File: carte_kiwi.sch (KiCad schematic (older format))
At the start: 40 parts, among them IC1 MCP2562, P1 CONN_01X05, P2 CONN_01X03, P3 CONN_01X05, P4 CONN_01X03, P5 Serial Wire, P6 CAN_conn, P7 CONN_01X03, P8 CONN_01X03, P9 CAN_conn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

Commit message: Mise à jour des libs (zener, led, switch)
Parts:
- removed D1, D2, D3: ZENERsmall, Diodes_SMD:SOD-123, symbol ZENERsmall
- removed SW1: SW_PUSH_SMALL_H, Buttons_Switches_SMD:SW_SPST_EVQPE1, symbol SW_PUSH_SMALL_H
- added D1, D2, D3: D_Zener_Small, Diodes_SMD:D_SOD-123, symbol D_Zener_Small
- added SW1: SW_Push, Buttons_Switches_SMD:SW_SPST_EVQPE1, symbol SW_Push
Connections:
- wire segments 65 -> 63
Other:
- moved on the sheet: C5, D4, D5, D6, P6, P9

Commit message: corrige erreurs ERC
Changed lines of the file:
@@
 LIBS:STMicroelectronics
 LIBS:switches
-LIBS:carte_kiwi-cache
 EELAYER 25 0
 EELAYER END
@@
 	0    1    1    0
 $EndComp
+$Comp
+L PWR_FLAG #FLG055
+U 1 1 589FF92C
+P 7400 5750
+F 0 "#FLG055" H 7400 5845 50  0001 C CNN
+F 1 "PWR_FLAG" H 7400 5950 50  0000 C CNN
+F 2 "" H 7400 5750 50  0000 C CNN
+F 3 "" H 7400 5750 50  0000 C CNN
+	1    7400 5750
+	1    0    0    -1
+$EndComp
+$Comp
+L GND #PWR056
+U 1 1 589FF9B6
+P 7400 5750
+F 0 "#PWR056" H 7400 5500 50  0001 C CNN
+F 1 "GND" H 7400 5600 50  0000 C CNN
+F 2 "" H 7400 5750 50  0000 C CNN
+F 3 "" H 7400 5750 50  0000 C CNN
+	1    7400 5750
+	1    0    0    -1
+$EndComp
+$Comp
+L +9V #PWR057
+U 1 1 589FFA61
+P 7800 5700
+F 0 "#PWR057" H 7800 5550 50  0001 C CNN
+F 1 "+9V" H 7800 5840 50  0000 C CNN
+F 2 "" H 7800 5700 50  0000 C CNN
+F 3 "" H 7800 5700 50  0000 C CNN
+	1    7800 5700
+	1    0    0    -1
+$EndComp
+$Comp
+L PWR_FLAG #FLG058
+U 1 1 589FFAE4
+P 7800 5700
+F 0 "#FLG058" H 7800 5795 50  0001 C CNN
+F 1 "PWR_FLAG" H 7800 5900 50  0000 C CNN
+F 2 "" H 7800 5700 50  0000 C CNN
+F 3 "" H 7800 5700 50  0000 C CNN
+	1    7800 5700
+	-1   0    0    1
+$EndComp
 $EndSCHEMATC

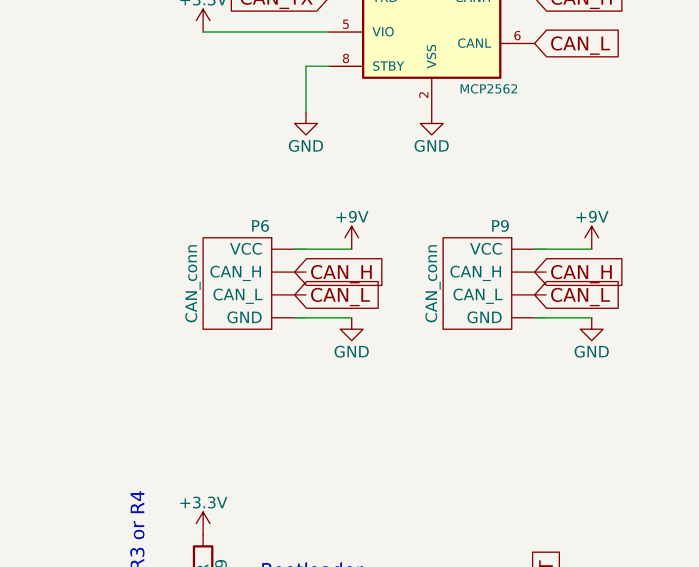
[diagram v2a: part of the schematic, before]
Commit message: retourné connecteur CAN
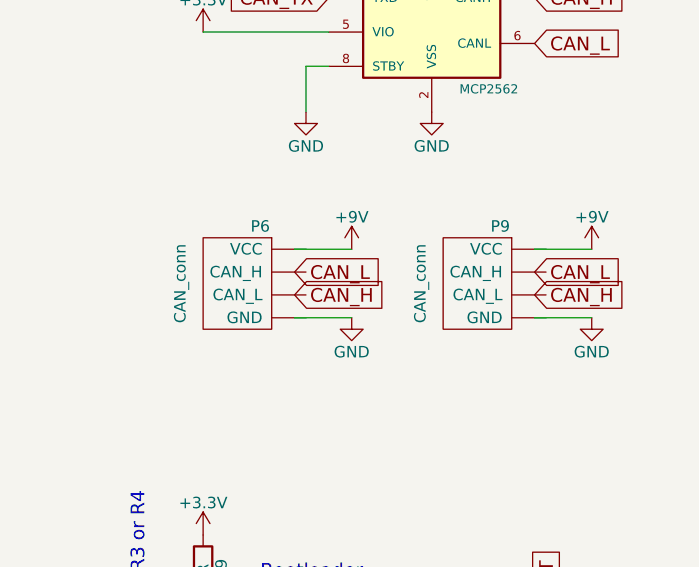
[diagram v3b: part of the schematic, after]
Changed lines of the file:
@@
 	-1   0    0    -1
 $EndComp
+Text GLabel 9400 3800 2    60   Input ~ 0
+CAN_H
 Text GLabel 9400 3700 2    60   Input ~ 0
-CAN_H
-Text GLabel 9400 3800 2    60   Input ~ 0
 CAN_L
 $Comp
@@
 Text GLabel 10500 5250 1    60   Input ~ 0
 NRST
+Text GLabel 10450 3800 2    60   Input ~ 0
+CAN_H
 Text GLabel 10450 3700 2    60   Input ~ 0
-CAN_H
-Text GLabel 10450 3800 2    60   Input ~ 0
 CAN_L
 $Comp
@@
 P 9250 3750
 F 0 "P6" H 9250 4000 50  0000 C CNN
-F 1 "CAN_conn" V 9550 3750 50  0000 C CNN
+F 1 "CAN_conn" V 9600 3750 50  0000 C CNN
 F 2 "Connectors_JST:JST_XH_B04B-XH-A_04x2.50mm_Straight" H 9250 3750 50  0001 C CNN
 F 3 "" H 9250 3750 50  0000 C CNN
@@
 P 10300 3750
 F 0 "P9" H 10300 4000 50  0000 C CNN
-F 1 "CAN_conn" V 10600 3750 50  0000 C CNN
+F 1 "CAN_conn" V 10650 3750 50  0000 C CNN
 F 2 "Connectors_JST:JST_XH_B04B-XH-A_04x2.50mm_Straight" H 10300 3750 50  0001 C CNN
 F 3 "" H 10300 3750 50  0000 C CNN

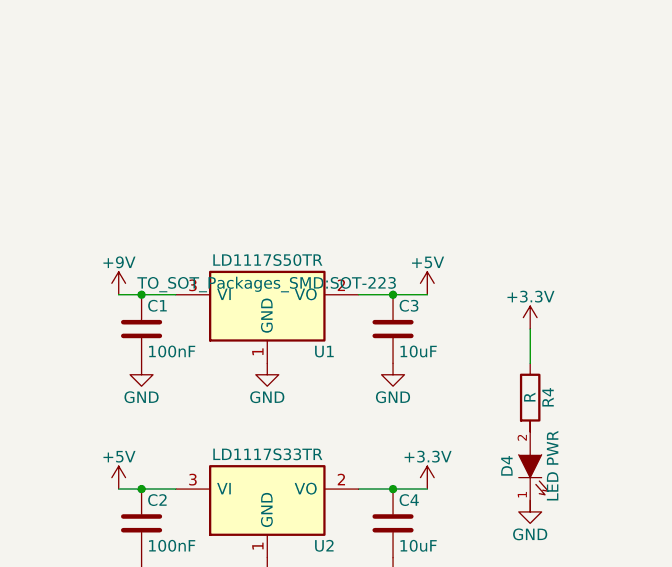
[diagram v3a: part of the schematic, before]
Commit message: updated footprint
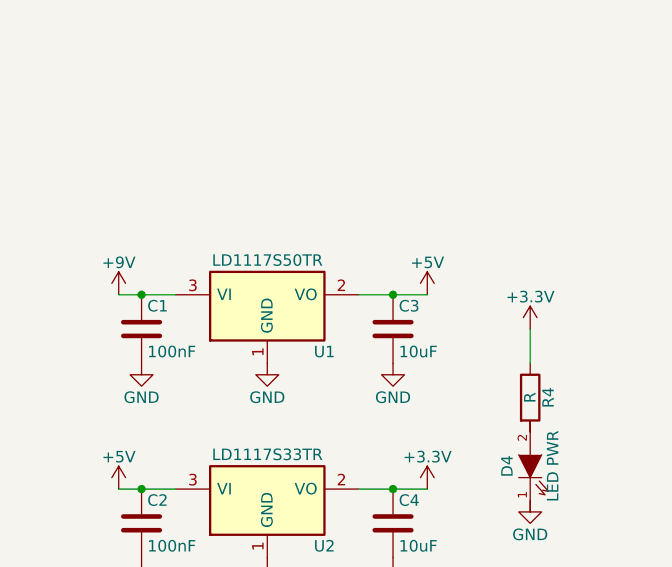
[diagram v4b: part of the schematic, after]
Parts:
- U1, U2: footprint TO_SOT_Packages_SMD:SOT-223 -> TO_SOT_Packages_SMD:SOT-223-3Lead_TabPin2
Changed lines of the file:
@@
 F 0 "U2" H 2050 6700 50  0000 C CNN
 F 1 "LD1117S33TR" H 1800 7100 50  0000 C CNN
-F 2 "TO_SOT_Packages_SMD:SOT-223" H 1800 7000 50  0001 C CNN
+F 2 "TO_SOT_Packages_SMD:SOT-223-3Lead_TabPin2" H 1800 7000 50  0001 C CNN
 F 3 "" H 1800 6900 50  0000 C CNN
 	1    1800 6900
@@
 F 0 "U1" H 2050 5850 50  0000 C CNN
 F 1 "LD1117S50TR" H 1800 6250 50  0000 C CNN
-F 2 "TO_SOT_Packages_SMD:SOT-223" H 1800 6150 50  0000 C CNN
+F 2 "TO_SOT_Packages_SMD:SOT-223-3Lead_TabPin2" H 1800 6150 50  0001 C CNN
 F 3 "" H 1800 6050 50  0000 C CNN
 	1    1800 6050

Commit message: First changes to schema. TODO : use phoenixrobotik specific libs for can_conn
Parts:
- C1, C10, C2, C3, C4, C5, C6, C7, C8, C9: symbol C -> Device:C
- D1, D2, D3: symbol D_Zener_Small -> Device:D_Zener_Small
- D4, D5, D6: symbol LED -> Device:LED
- IC1: symbol MCP2562 -> Interface_CAN_LIN:MCP2562-E-P
- P1, P3: value CONN_01X05 -> Connector_Generic:Conn_01x05; symbol CONN_01X05 -> Connector_Generic:Conn_01x05
- P2, P4, P7, P8: value CONN_01X03 -> Connector_Generic:Conn_01x03; symbol CONN_01X03 -> Connector_Generic:Conn_01x03
- P5: symbol CONN_01X06 -> Connector_Generic:Conn_01x06
- P6, P9: symbol CAN_conn -> Connector_Generic:Conn_01x04
- R1, R10, R2, R3, R4, R5, R6, R7, R8, R9: symbol R -> Device:R
- SW1: symbol SW_Push -> Switch:SW_Push
- U1: symbol LD1117S50TR -> Regulator_Linear:LD1117S50TR_SOT223
- U2: symbol LD1117S33TR -> Regulator_Linear:LD1117S33TR_SOT223
- U3: symbol STM32F303K8 -> MCU_ST_STM32F3:STM32F303K8Tx
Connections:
- wire segments 63 -> 66
